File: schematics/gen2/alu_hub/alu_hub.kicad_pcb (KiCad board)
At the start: 2 copper layers, 100 x 91.1 mm, 24 parts, among them U1 74LS574, U10 74LS02, U2 74LS245, U3 74LS02, U4 74LS181, U5 74LS181, U6 74LS574, U7 74LS245, U8 74LS245, U9 74LS02

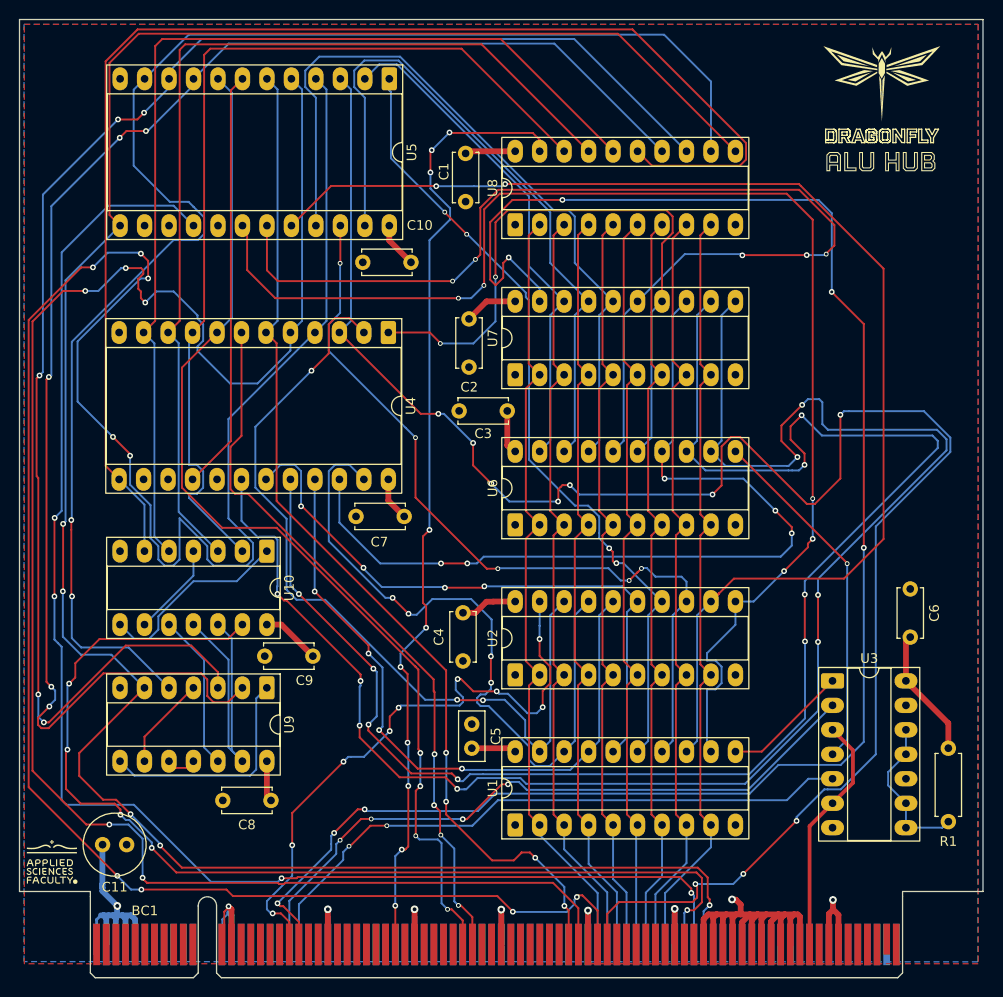
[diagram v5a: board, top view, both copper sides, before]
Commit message: fix(kicad): vcc zones
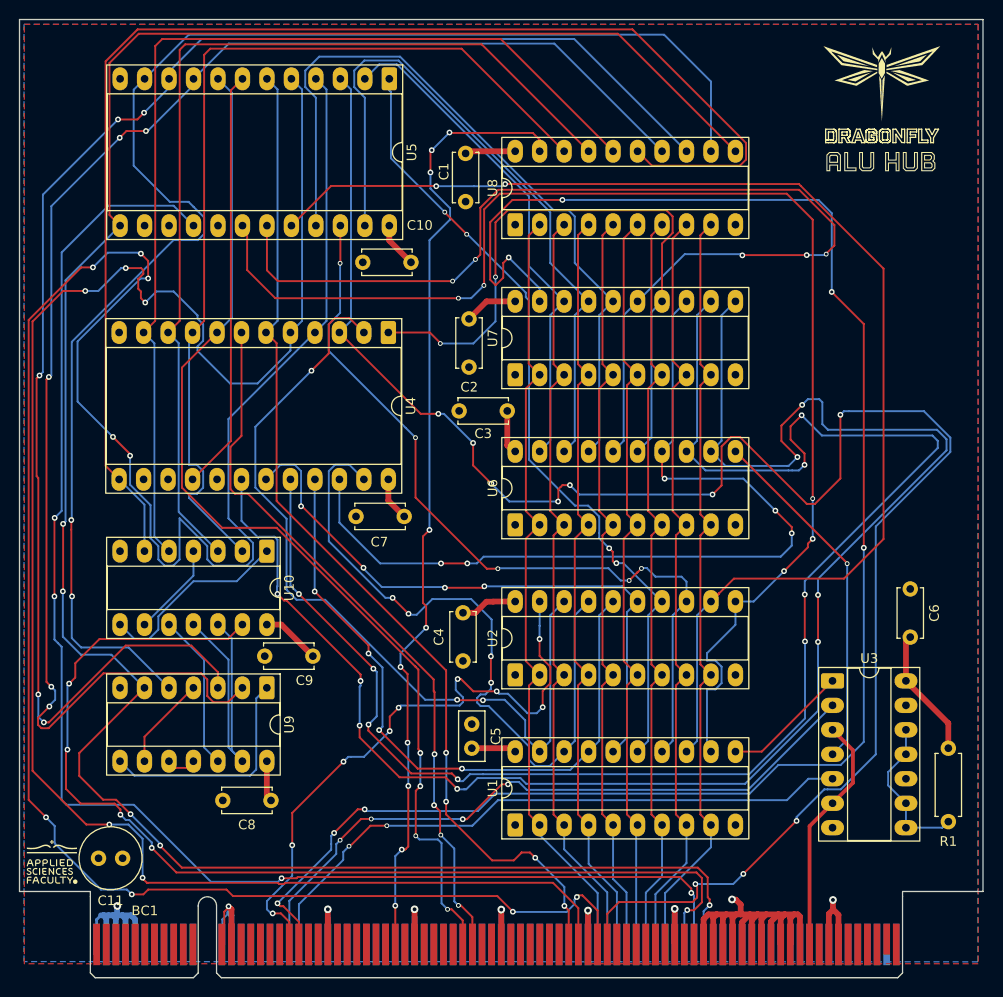
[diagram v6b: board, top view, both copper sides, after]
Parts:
- moved C11 1.47 mm to (110.7, 131.6)
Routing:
- net VCC: track 87.0 -> 78.8 mm
- net Net-(BC1-ALUS2): track 245.0 -> 247.3 mm
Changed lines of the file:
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@@
 			(pinfunction "VCC")
 			(pintype "power_in")
+			(zone_connect 0)
 		)
 		(embedded_fonts no)
@@
 			(pinfunction "VCC")
 			(pintype "power_in")
+			(zone_connect 0)
 		)
 		(embedded_fonts no)
@@
 			(pinfunction "VCC")
 			(pintype "power_in")
+			(zone_connect 0)
 		)
 		(embedded_fonts no)
@@
 	(footprint "Capacitor_THT:C_Radial_D6.3mm_H5.0mm_P2.50mm"
 		(layer "F.Cu")
-		(at 111.12 130.14 180)
+		(at 110.7 131.55 180)
 		(descr "C, Radial series, Radial, pin pitch=2.50mm, diameter=6.3mm, height=5mm, Non-Polar Electrolytic Capacitor")
 		(tags "C Radial series Radial pin pitch 2.50mm diameter 6.3mm height 5mm Non-Polar Electrolytic Capacitor")
@@
 			(pinfunction "VCC")
 			(pintype "power_in")
+			(zone_connect 0)
 		)
 		(embedded_fonts no)
@@
 			(pinfunction "VCC")
 			(pintype "power_in")
+			(zone_connect 0)
 		)
 		(embedded_fonts no)
@@
 			(pinfunction "VCC")
 			(pintype "power_in")
+			(zone_connect 0)
 		)
 		(embedded_fonts no)
@@
 			(pinfunction "VCC")
 			(pintype "power_in")
+			(zone_connect 0)
 		)
 		(embedded_fonts no)
@@
 			(pinfunction "VCC")
 			(pintype "power_in")
+			(zone_connect 0)
 		)
 		(embedded_fonts no)
@@
 			(pinfunction "VCC")
 			(pintype "power_in")
+			(zone_connect 0)
 		)
 		(embedded_fonts no)
@@
 			(pinfunction "VCC")
 			(pintype "power_in")
+			(zone_connect 0)
 		)
 		(embedded_fonts no)
@@
 	)
 	(segment
-		(start 192.47 112.67)
-		(end 192 113.14)
-		(width 0.6)
-		(layer "F.Cu")
-		(net 2)
-	)
-	(segment
 		(start 148.4625 104.925)
 		(end 147.3125 106.075)
@@
 	)
 	(segment
-		(start 108.625 134.65)
-		(end 108.6 134.625)
-		(width 0.6)
-		(layer "B.Cu")
-		(net 2)
-	)
-	(segment
 		(start 111 140.525)
 		(end 111 140.5)
@@
 	)
 	(segment
-		(start 108.6 134.95)
-		(end 110.15 136.5)
-		(width 0.6)
-		(layer "B.Cu")
-		(net 2)
-	)
-	(segment
 		(start 110 137.775)
 		(end 109.7 137.475)
@@
 	)
 	(segment
-		(start 108.6 134.625)
-		(end 108.6 134.25)
-		(width 0.6)
-		(layer "B.Cu")
-		(net 2)
-	)
-	(segment
 		(start 111 140.5)
 		(end 111 137.8)
@@
 	)
 	(segment
-		(start 108.6 134.25)
-		(end 108.6 134.95)
-		(width 0.6)
-		(layer "B.Cu")
-		(net 2)
-	)
-	(segment
-		(start 108.6 134.25)
-		(end 108.6 130)
-		(width 0.6)
-		(layer "B.Cu")
-		(net 2)
-	)
-	(segment
 		(start 108.725 137.475)
 		(end 109.25 137.475)
@@
 	)
 	(segment
-		(start 149.591364 135.475)
-		(end 122.15 135.475)
+		(start 106.4079 70.225)
+		(end 107.625 70.225)
 		(width 0.2)
 		(layer "F.Cu")
@@
 	)
 	(segment
-		(start 121.475 134.8)
-		(end 112.65 134.8)
+		(start 113.35 134.8)
+		(end 121.475 134.8)
 		(width 0.2)
 		(layer "F.Cu")
@@
 	)
 	(segment
-		(start 111.475 89.6)
-		(end 111.475 89.775)
+		(start 151.2 137.083636)
+		(end 151.2 137.1)
 		(width 0.2)
 		(layer "F.Cu")
@@
 	)
 	(segment
-		(start 158.416364 135.4)
-		(end 160 136.983636)
+		(start 122.15 135.475)
+		(end 149.591364 135.475)
 		(width 0.2)
 		(layer "F.Cu")
@@
 	)
 	(segment
-		(start 106.4079 70.225)
-		(end 107.625 70.225)
+		(start 121.475 134.8)
+		(end 122.15 135.475)
 		(width 0.2)
 		(layer "F.Cu")
@@
 	)
 	(segment
-		(start 151.2 137.083636)
-		(end 149.591364 135.475)
+		(start 149.591364 135.475)
+		(end 151.2 137.083636)
 		(width 0.2)
 		(layer "F.Cu")
@@
 	)
 	(segment
-		(start 110.15 133.375)
-		(end 100.948 124.173)
+		(start 111.475 89.6)
+		(end 111.475 89.775)
+		(width 0.2)
+		(layer "F.Cu")
+		(net 84)
+	)
+	(segment
+		(start 158.416364 135.4)
+		(end 160 136.983636)
 		(width 0.2)
 		(layer "F.Cu")
@@
 	)
 	(segment
-		(start 157.85 135.575)
-		(end 158.025 135.4)
+		(start 100.948 75.6849)
+		(end 106.4079 70.225)
 		(width 0.2)
 		(layer "F.Cu")
@@
 	)
 	(segment
-		(start 113.35 69.55)
-		(end 113.35 71.375)
+		(start 111.65 135.3)
+		(end 112.85 135.3)
 		(width 0.2)
 		(layer "F.Cu")
@@
 	)
 	(segment
-		(start 100.948 124.173)
-		(end 100.948 75.6849)
+		(start 157.85 135.575)
+		(end 158.025 135.4)
 		(width 0.2)
 		(layer "F.Cu")
@@
 	)
 	(segment
-		(start 122.15 135.475)
-		(end 121.475 134.8)
+		(start 113.35 69.55)
+		(end 113.35 71.375)
 		(width 0.2)
 		(layer "F.Cu")
@@
 	)
 	(segment
+		(start 100.948 125.498)
+		(end 100.948 75.6849)
+		(width 0.2)
+		(layer "F.Cu")
+		(net 84)
+	)
+	(segment
 		(start 112.6 68.8)
 		(end 113.35 69.55)
@@
 	)
 	(segment
-		(start 100.948 75.6849)
-		(end 106.4079 70.225)
+		(start 102.75 127.3)
+		(end 100.948 125.498)
 		(width 0.2)
 		(layer "F.Cu")
@@
 	)
 	(segment
-		(start 160 136.983636)
-		(end 160 140.5)
+		(start 112.85 135.3)
+		(end 113.35 134.8)
 		(width 0.2)
 		(layer "F.Cu")
@@
 	)
 	(segment
-		(start 151.2 137.1)
-		(end 151.2 137.083636)
+		(start 160 136.983636)
+		(end 160 140.5)
 		(width 0.2)
 		(layer "F.Cu")
@@
 	)
 	(via
-		(at 110.15 133.375)
+		(at 102.75 127.3)
 		(size 0.6)
 		(drill 0.3)
@@
 	)
 	(via
-		(at 112.65 134.8)
+		(at 111.65 135.3)
 		(size 0.6)
 		(drill 0.3)
@@
 	)
 	(segment
+		(start 111.15 134.8)
+		(end 108.45 134.8)
+		(width 0.2)
+		(layer "B.Cu")
+		(net 84)
+	)
+	(segment
 		(start 121.6839 85.9611)
 		(end 130.66 76.985)
@@
 	)
 	(segment
+		(start 111.65 135.3)
+		(end 111.15 134.8)
+		(width 0.2)
+		(layer "B.Cu")
+		(net 84)
+	)
+	(segment
 		(start 119.489 100.536049)
 		(end 120.133951 101.181)
@@
 	)
 	(segment
-		(start 111.575 134.8)
-		(end 112.65 134.8)
-		(width 0.2)
-		(layer "B.Cu")
-		(net 84)
-	)
-	(segment
 		(start 109.15 68.7)
 		(end 112.3 68.7)
@@
 	)
 	(segment
-		(start 110.15 133.375)
-		(end 111.575 134.8)
-		(width 0.2)
-		(layer "B.Cu")
-		(net 84)
-	)
-	(segment
 		(start 115.053951 101.181)
 		(end 115.966049 101.181)
@@
 	)
 	(segment
+		(start 103.65 130)
+		(end 103.65 128.2)
+		(width 0.2)
+		(layer "B.Cu")
+		(net 84)
+	)
+	(segment
 		(start 112.5 68.7)
 		(end 112.6 68.8)
@@
 	)
 	(segment
+		(start 103.65 128.2)
+		(end 102.75 127.3)
+		(width 0.2)
+		(layer "B.Cu")
+		(net 84)
+	)
+	(segment
 		(start 156.774943 137.125)
 		(end 151.241364 137.125)
 		(width 0.2)
 		(layer "B.Cu")
+		(net 84)
+	)
+	(segment
+		(start 108.45 134.8)
+		(end 103.65 130)
+		(width 0.2)
+		(layer "B.Cu")

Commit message: fix(alu)
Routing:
- net Net-(BC1-ALUS2): track 247.3 -> 244.0 mm
- net /HIGH7: track 138.3 -> 136.0 mm
- net Net-(BC1-ALUS1): track 186.0 -> 183.7 mm
- net Net-(BC1-~{RARGH}): track 64.9 -> 62.7 mm
- net Net-(U4-F0): track 98.7 -> 97.0 mm
- net /LOW7: track 172.5 -> 171.0 mm
- net Net-(BC1-ALUSO): track 233.4 -> 232.4 mm
- net Net-(BC1-~{ALUCO}): track 149.5 -> 150.2 mm
- net Net-(BC1-~{LARGH}): track 70.6 -> 70.0 mm
